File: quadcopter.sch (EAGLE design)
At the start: 70 parts, among them J1 AVR_SPI_PRG_6NS, SW1 PUSHBUTTON_SMD-VERTICAL-1, U1 ATMEGA128RFA1, Y2 16MHz

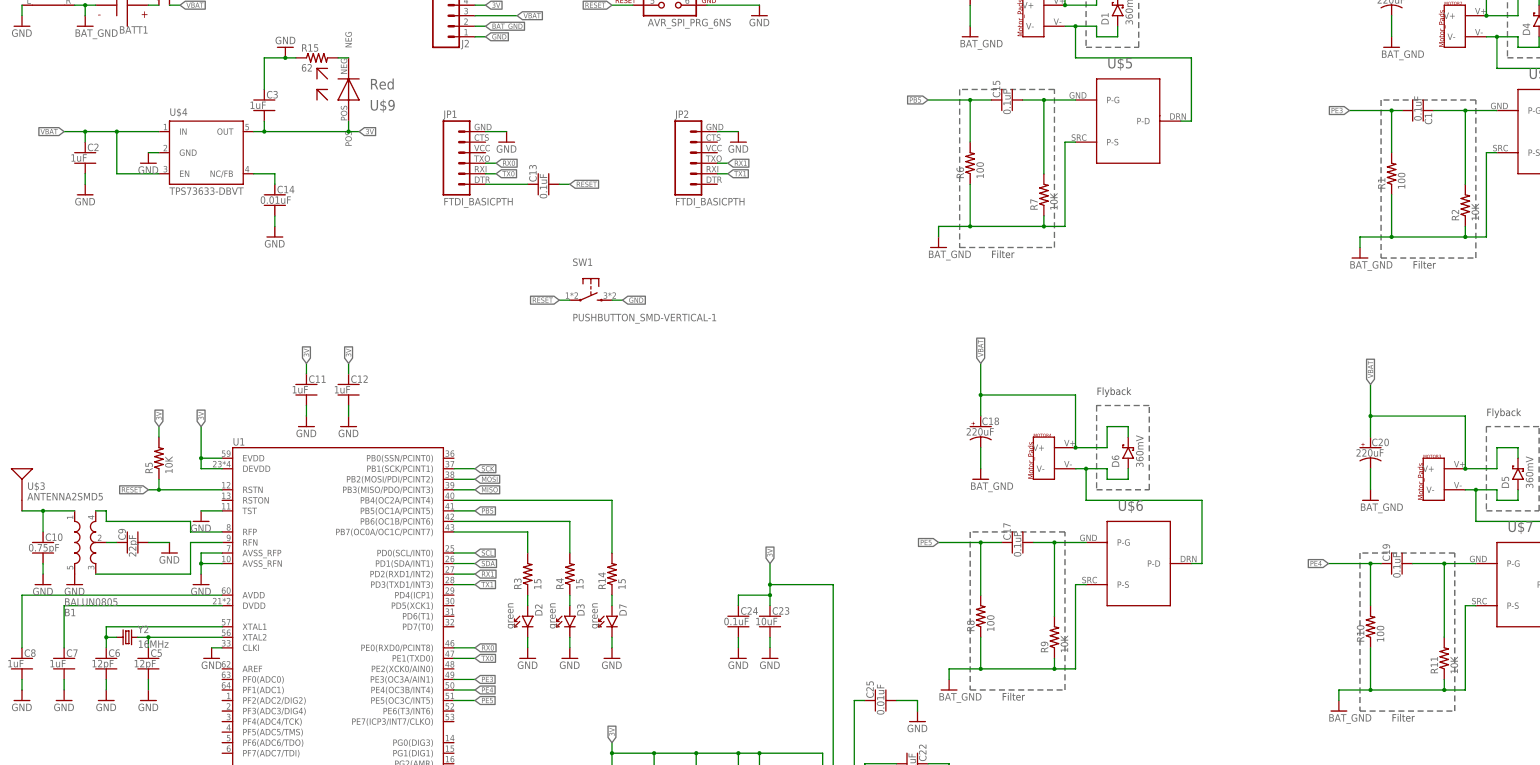
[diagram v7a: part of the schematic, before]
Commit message: Fixed additional issues found by Swanson in schematic
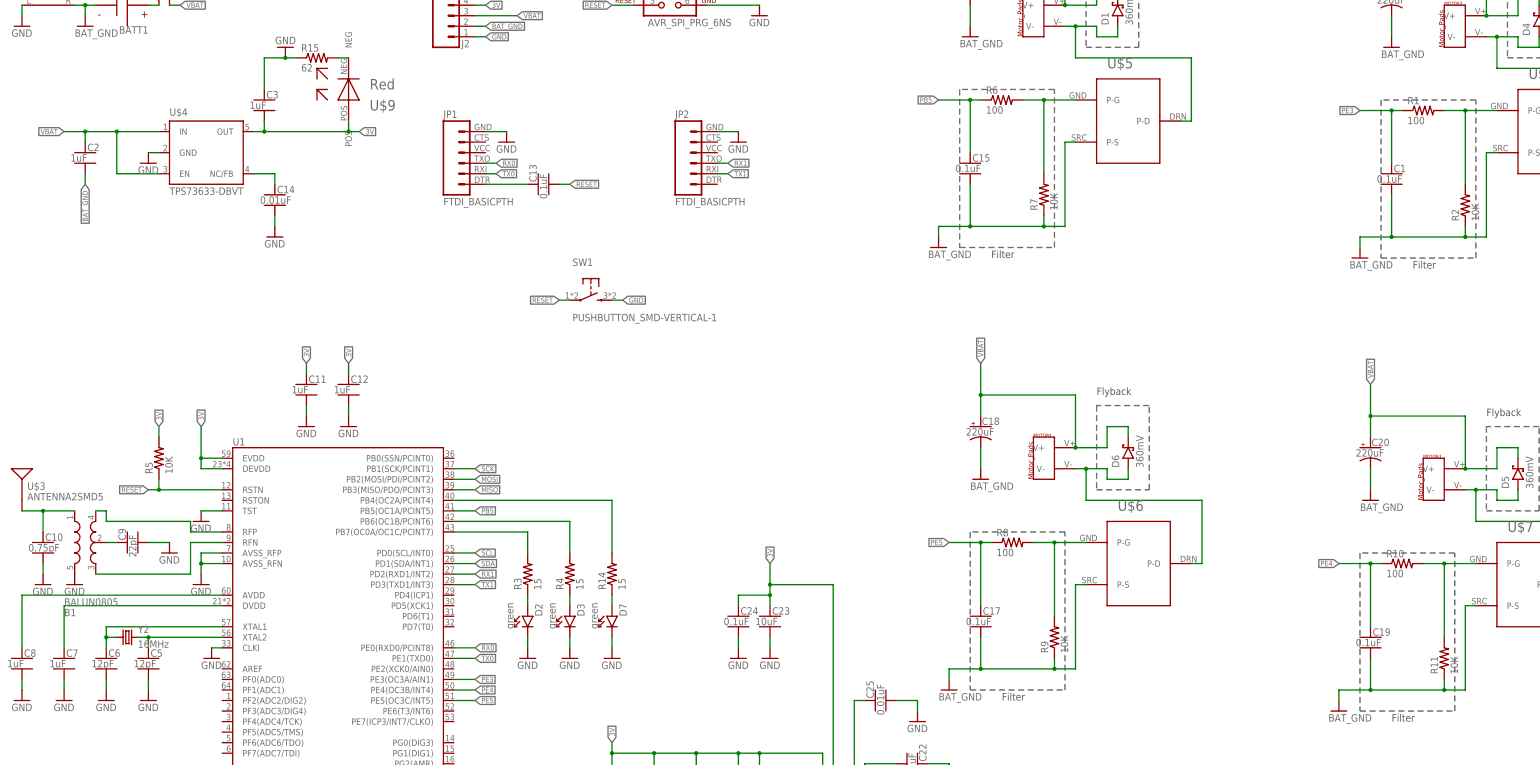
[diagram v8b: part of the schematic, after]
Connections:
- net BAT_GND: now also C1.2, C15.2, C17.2, C19.2, C2.2; no longer R1.1, R10.1, R6.1, R8.1
- net FILTERED1: now also R6.2; no longer C15.2
- net FILTERED2: now also R1.2; no longer C1.1
- net FILTERED3: now also R10.2; no longer C19.2
- net FILTERED4: now also R8.2; no longer C17.2
- net GND: no longer C2.2
- net PB5: now also R6.1; no longer R6.2
- net PE3: now also C1.1, R1.1; no longer C1.2, R1.2
- net PE4: now also R10.1; no longer R10.2
- net PE5: now also R8.1; no longer R8.2
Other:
- moved on the sheet: C1, C15, C17, C19, R1, R10, R6, R8
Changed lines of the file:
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@@
 <part name="U$4" library="quadparts_prebuilt" deviceset="TPS73633-DBVT" device=""/>
 <part name="C2" library="quadparts_prebuilt" deviceset="CAPACITOR-NP_" device="SMD-2012-0805_CERAMIC-1UF" value="1uF"/>
-<part name="GND3" library="quadparts_prebuilt" deviceset="GND" device=""/>
 <part name="GND4" library="quadparts_prebuilt" deviceset="GND" device=""/>
 <part name="GND20" library="quadparts_prebuilt" deviceset="GND" device=""/>
@@
 </plain>
 <instances>
-<instance part="R1" gate="G$1" x="363.22" y="200.66" rot="R90"/>
+<instance part="R1" gate="G$1" x="370.84" y="215.9"/>
 <instance part="R2" gate="G$1" x="381" y="193.04" rot="R90"/>
 <instance part="GND1" gate="1" x="363.22" y="231.14"/>
@@
 <instance part="U$4" gate="G$1" x="68.58" y="198.12"/>
 <instance part="C2" gate="G$1" x="48.26" y="205.74"/>
-<instance part="GND3" gate="1" x="48.26" y="195.58"/>
 <instance part="GND4" gate="1" x="93.98" y="185.42"/>
 <instance part="GND20" gate="1" x="96.52" y="231.14" rot="R180"/>
@@
 <instance part="J2" gate="G$1" x="132.08" y="231.14"/>
 <instance part="J3" gate="G$1" x="63.5" y="251.46" rot="R270"/>
-<instance part="R6" gate="G$1" x="261.62" y="203.2" rot="R90"/>
+<instance part="R6" gate="G$1" x="269.24" y="218.44"/>
 <instance part="R7" gate="G$1" x="279.4" y="195.58" rot="R90"/>
 <instance part="GND27" gate="1" x="261.62" y="233.68"/>
@@
 <instance part="GND28" gate="1" x="254" y="182.88"/>
 <instance part="U$5" gate="G$1" x="299.72" y="213.36"/>
-<instance part="R8" gate="G$1" x="264.16" y="93.98" rot="R90"/>
+<instance part="R8" gate="G$1" x="271.78" y="111.76"/>
 <instance part="R9" gate="G$1" x="281.94" y="88.9" rot="R90"/>
 <instance part="GND29" gate="1" x="264.16" y="127"/>
@@
 <instance part="GND30" gate="1" x="256.54" y="76.2"/>
 <instance part="U$6" gate="G$1" x="302.26" y="106.68"/>
-<instance part="R10" gate="G$1" x="358.14" y="91.44" rot="R90"/>
+<instance part="R10" gate="G$1" x="365.76" y="106.68"/>
 <instance part="R11" gate="G$1" x="375.92" y="83.82" rot="R90"/>
 <instance part="GND31" gate="1" x="358.14" y="121.92"/>
@@
 <instance part="C25" gate="G$1" x="238.76" y="73.66" rot="R90"/>
 <instance part="C22" gate="G$1" x="248.92" y="58.42" rot="MR90"/>
-<instance part="C15" gate="G$1" x="269.24" y="218.44" rot="R90"/>
-<instance part="C1" gate="G$1" x="370.84" y="215.9" rot="R270"/>
-<instance part="C17" gate="G$1" x="271.78" y="111.76" rot="R90"/>
-<instance part="C19" gate="G$1" x="363.22" y="106.68" rot="R90"/>
+<instance part="C15" gate="G$1" x="261.62" y="203.2"/>
+<instance part="C1" gate="G$1" x="363.22" y="200.66"/>
+<instance part="C17" gate="G$1" x="264.16" y="93.98"/>
+<instance part="C19" gate="G$1" x="358.14" y="88.9"/>
 <instance part="SW1" gate="G$1" x="170.18" y="172.72"/>
 </instances>
@@
 </segment>
 <segment>
-<pinref part="C2" gate="G$1" pin="2"/>
-<pinref part="GND3" gate="1" pin="GND"/>
-<wire x1="48.26" y1="198.12" x2="48.26" y2="200.66" width="0.1524" layer="91"/>
-</segment>
-<segment>
 <pinref part="C14" gate="G$1" pin="2"/>
 <pinref part="GND4" gate="1" pin="GND"/>
@@
 <pinref part="R9" gate="G$1" pin="2"/>
 <wire x1="281.94" y1="93.98" x2="281.94" y2="111.76" width="0.1524" layer="91"/>
-<pinref part="C17" gate="G$1" pin="2"/>
+<pinref part="R8" gate="G$1" pin="2"/>
 <wire x1="276.86" y1="111.76" x2="281.94" y2="111.76" width="0.1524" layer="91"/>
 <junction x="281.94" y="111.76"/>
@@
 </segment>
 <segment>
-<pinref part="R6" gate="G$1" pin="2"/>
-<wire x1="261.62" y1="208.28" x2="261.62" y2="218.44" width="0.1524" layer="91"/>
 <pinref part="C15" gate="G$1" pin="1"/>
-<wire x1="261.62" y1="218.44" x2="266.7" y2="218.44" width="0.1524" layer="91"/>
-<wire x1="261.62" y1="218.44" x2="251.46" y2="218.44" width="0.1524" layer="91"/>
+<wire x1="261.62" y1="205.74" x2="261.62" y2="218.44" width="0.1524" layer="91"/>
+<pinref part="R6" gate="G$1" pin="1"/>
+<wire x1="261.62" y1="218.44" x2="264.16" y2="218.44" width="0.1524" layer="91"/>
+<wire x1="261.62" y1="218.44" x2="254" y2="218.44" width="0.1524" layer="91"/>
 <junction x="261.62" y="218.44"/>
-<label x="251.46" y="218.44" size="1.27" layer="95" rot="R180" xref="yes"/>
+<label x="254" y="218.44" size="1.27" layer="95" rot="R180" xref="yes"/>
 </segment>
 </net>
@@
 </segment>
 <segment>
-<pinref part="R1" gate="G$1" pin="2"/>
-<wire x1="363.22" y1="205.74" x2="363.22" y2="215.9" width="0.1524" layer="91"/>
-<pinref part="C1" gate="G$1" pin="2"/>
+<pinref part="C1" gate="G$1" pin="1"/>
+<wire x1="363.22" y1="203.2" x2="363.22" y2="215.9" width="0.1524" layer="91"/>
+<pinref part="R1" gate="G$1" pin="1"/>
 <wire x1="363.22" y1="215.9" x2="365.76" y2="215.9" width="0.1524" layer="91"/>
-<wire x1="363.22" y1="215.9" x2="353.06" y2="215.9" width="0.1524" layer="91"/>
+<wire x1="363.22" y1="215.9" x2="355.6" y2="215.9" width="0.1524" layer="91"/>
 <junction x="363.22" y="215.9"/>
-<label x="353.06" y="215.9" size="1.27" layer="95" rot="R180" xref="yes"/>
+<label x="355.6" y="215.9" size="1.27" layer="95" rot="R180" xref="yes"/>
 </segment>
 </net>
@@
 </segment>
 <segment>
-<pinref part="R10" gate="G$1" pin="2"/>
-<wire x1="358.14" y1="96.52" x2="358.14" y2="106.68" width="0.1524" layer="91"/>
 <pinref part="C19" gate="G$1" pin="1"/>
+<wire x1="358.14" y1="91.44" x2="358.14" y2="106.68" width="0.1524" layer="91"/>
+<pinref part="R10" gate="G$1" pin="1"/>
 <wire x1="358.14" y1="106.68" x2="360.68" y2="106.68" width="0.1524" layer="91"/>
-<wire x1="358.14" y1="106.68" x2="347.98" y2="106.68" width="0.1524" layer="91"/>
+<wire x1="358.14" y1="106.68" x2="350.52" y2="106.68" width="0.1524" layer="91"/>
 <junction x="358.14" y="106.68"/>
-<label x="347.98" y="106.68" size="1.27" layer="95" rot="R180" xref="yes"/>
+<label x="350.52" y="106.68" size="1.27" layer="95" rot="R180" xref="yes"/>
 </segment>
 </net>
@@
 <segment>
 <pinref part="C17" gate="G$1" pin="1"/>
-<wire x1="269.24" y1="111.76" x2="264.16" y2="111.76" width="0.1524" layer="91"/>
-<pinref part="R8" gate="G$1" pin="2"/>
-<wire x1="264.16" y1="111.76" x2="254" y2="111.76" width="0.1524" layer="91"/>
-<wire x1="264.16" y1="111.76" x2="264.16" y2="99.06" width="0.1524" layer="91"/>
+<wire x1="264.16" y1="96.52" x2="264.16" y2="111.76" width="0.1524" layer="91"/>
+<pinref part="R8" gate="G$1" pin="1"/>
+<wire x1="264.16" y1="111.76" x2="266.7" y2="111.76" width="0.1524" layer="91"/>
+<wire x1="264.16" y1="111.76" x2="256.54" y2="111.76" width="0.1524" layer="91"/>
 <junction x="264.16" y="111.76"/>
-<label x="254" y="111.76" size="1.27" layer="95" rot="R180" xref="yes"/>
+<label x="256.54" y="111.76" size="1.27" layer="95" rot="R180" xref="yes"/>
 </segment>
 </net>
@@
 <wire x1="281.94" y1="83.82" x2="281.94" y2="81.28" width="0.1524" layer="91"/>
 <junction x="281.94" y="81.28"/>
-<pinref part="R8" gate="G$1" pin="1"/>
+<pinref part="C17" gate="G$1" pin="2"/>
 <wire x1="264.16" y1="88.9" x2="264.16" y2="81.28" width="0.1524" layer="91"/>
 <junction x="264.16" y="81.28"/>
@@
 <wire x1="279.4" y1="190.5" x2="279.4" y2="187.96" width="0.1524" layer="91"/>
 <junction x="279.4" y="187.96"/>
-<pinref part="R6" gate="G$1" pin="1"/>
+<pinref part="C15" gate="G$1" pin="2"/>
 <wire x1="261.62" y1="198.12" x2="261.62" y2="187.96" width="0.1524" layer="91"/>
 <junction x="261.62" y="187.96"/>
@@
 <wire x1="375.92" y1="78.74" x2="375.92" y2="76.2" width="0.1524" layer="91"/>
 <junction x="375.92" y="76.2"/>
-<pinref part="R10" gate="G$1" pin="1"/>
-<wire x1="358.14" y1="86.36" x2="358.14" y2="76.2" width="0.1524" layer="91"/>
+<pinref part="C19" gate="G$1" pin="2"/>
+<wire x1="358.14" y1="83.82" x2="358.14" y2="76.2" width="0.1524" layer="91"/>
 <junction x="358.14" y="76.2"/>
 </segment>
@@
 <wire x1="381" y1="187.96" x2="381" y2="185.42" width="0.1524" layer="91"/>
 <junction x="381" y="185.42"/>
-<pinref part="R1" gate="G$1" pin="1"/>
+<pinref part="C1" gate="G$1" pin="2"/>
 <wire x1="363.22" y1="195.58" x2="363.22" y2="185.42" width="0.1524" layer="91"/>
 <junction x="363.22" y="185.42"/>
@@
 <wire x1="48.26" y1="238.76" x2="48.26" y2="241.3" width="0.1524" layer="91"/>
 <junction x="48.26" y="241.3"/>
+</segment>
+<segment>
+<pinref part="C2" gate="G$1" pin="2"/>
+<wire x1="48.26" y1="198.12" x2="48.26" y2="200.66" width="0.1524" layer="91"/>
+<label x="48.26" y="198.12" size="1.27" layer="95" rot="R270" xref="yes"/>
 </segment>
 </net>
@@
 <pinref part="R7" gate="G$1" pin="2"/>
 <wire x1="279.4" y1="200.66" x2="279.4" y2="218.44" width="0.1524" layer="91"/>
-<pinref part="C15" gate="G$1" pin="2"/>
+<pinref part="R6" gate="G$1" pin="2"/>
 <wire x1="274.32" y1="218.44" x2="279.4" y2="218.44" width="0.1524" layer="91"/>
 <junction x="279.4" y="218.44"/>
@@
 <pinref part="R2" gate="G$1" pin="2"/>
 <wire x1="381" y1="198.12" x2="381" y2="215.9" width="0.1524" layer="91"/>
-<pinref part="C1" gate="G$1" pin="1"/>
-<wire x1="373.38" y1="215.9" x2="381" y2="215.9" width="0.1524" layer="91"/>
+<pinref part="R1" gate="G$1" pin="2"/>
+<wire x1="375.92" y1="215.9" x2="381" y2="215.9" width="0.1524" layer="91"/>
 <junction x="381" y="215.9"/>
 </segment>
@@
 <pinref part="R11" gate="G$1" pin="2"/>
 <wire x1="375.92" y1="88.9" x2="375.92" y2="106.68" width="0.1524" layer="91"/>
-<pinref part="C19" gate="G$1" pin="2"/>
-<wire x1="368.3" y1="106.68" x2="375.92" y2="106.68" width="0.1524" layer="91"/>
+<pinref part="R10" gate="G$1" pin="2"/>
+<wire x1="370.84" y1="106.68" x2="375.92" y2="106.68" width="0.1524" layer="91"/>
 <junction x="375.92" y="106.68"/>
 </segment>
